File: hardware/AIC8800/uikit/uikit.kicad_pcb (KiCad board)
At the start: 2 copper layers, 50.8 x 69.2 mm, 48 parts, among them J1 Conn_01x20, J2 Conn_01x20, J3 Conn_01x10, J4 Conn_01x06, J5 USB_C_Receptacle_USB2.0, J6 Micro_SD_Card_Det, J7 PJ-393-USA, U1 AIC1000A, U2 CH340N, U3 NS8002

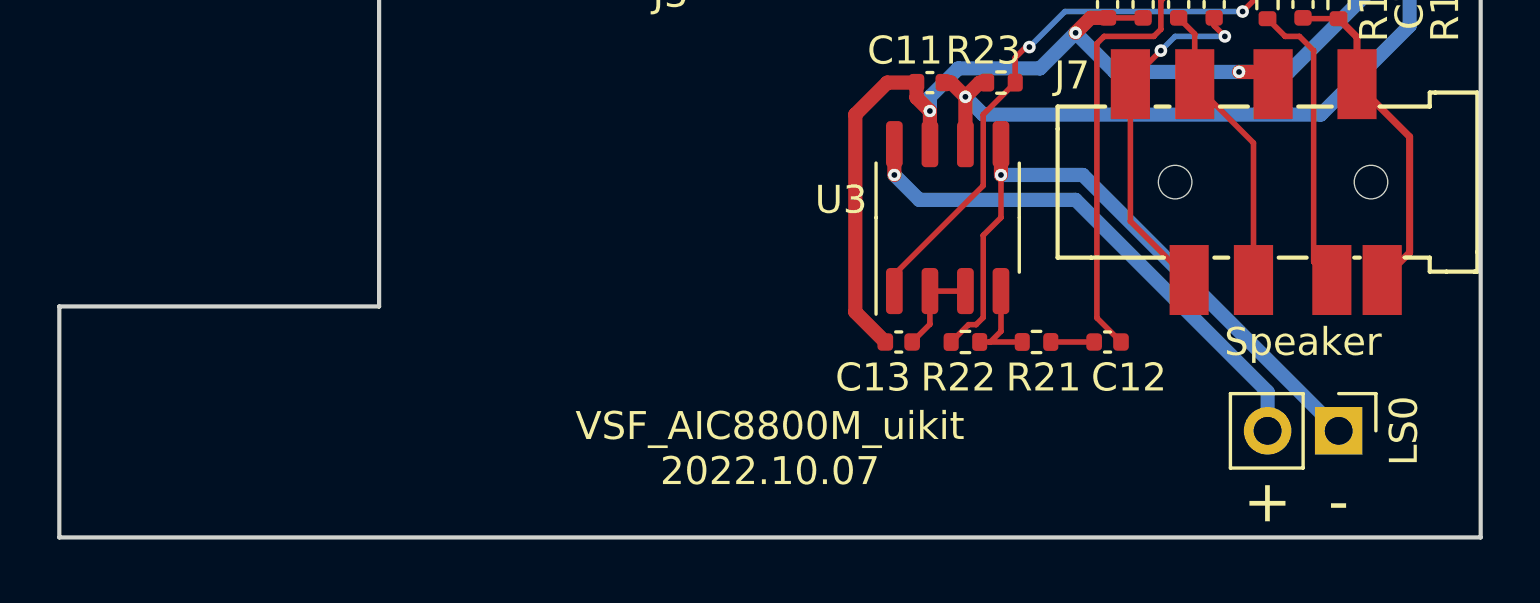
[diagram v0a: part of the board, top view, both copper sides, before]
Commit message: [hardware/aic8800/uikit] update microphone position
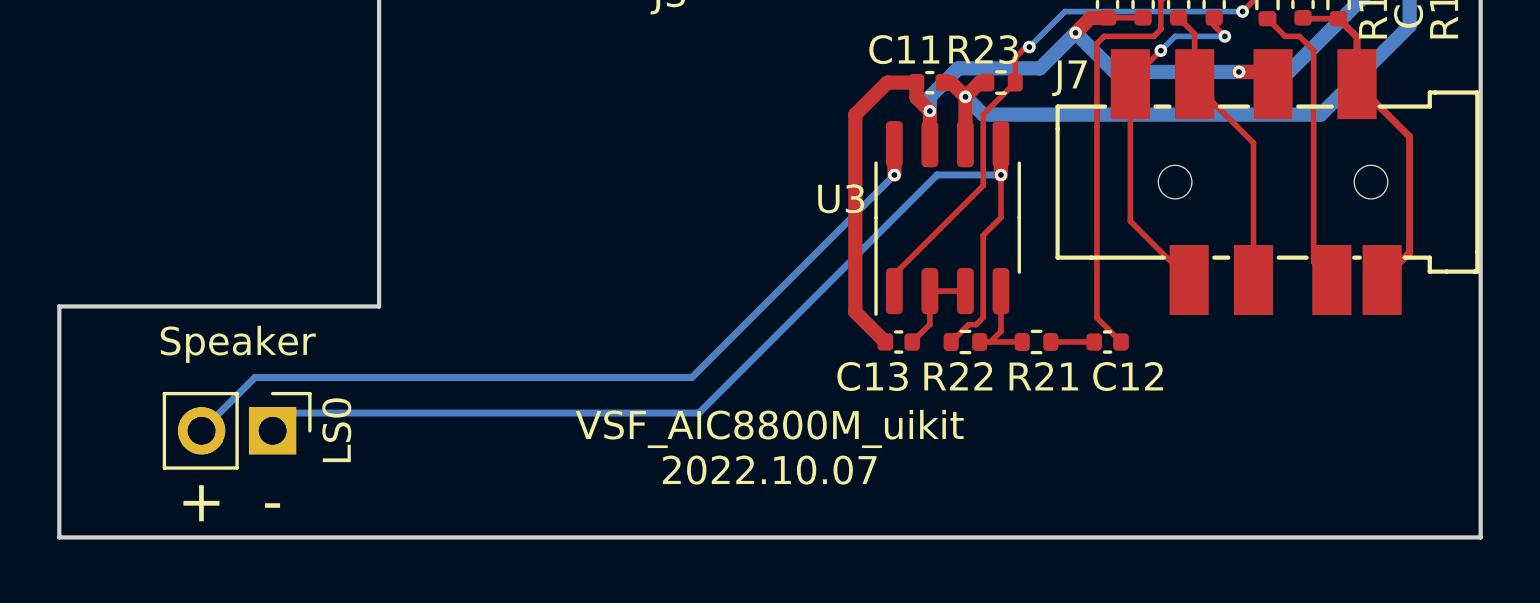
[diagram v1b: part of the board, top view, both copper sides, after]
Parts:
- moved LS0 38.1 mm to (210.8, 154.3)
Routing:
- net Net-(LS0-Pad1): track 23.8 -> 37.8 mm
- net Net-(LS0-Pad2): track 19.0 -> 29.6 mm
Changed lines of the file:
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@@
   )
   (footprint "Connector_PinHeader_2.54mm:PinHeader_1x02_P2.54mm_Vertical" (layer "F.Cu")
-    (at 248.925 154.305 -90)
+    (at 210.825 154.305 -90)
     (descr "Through hole straight pin header, 1x02, 2.54mm pitch, single row")
     (tags "Through hole pin header THT 1x02 2.54mm single row")
@@
   (gr_line (start 254 88.9) (end 254 119.888) (layer "Edge.Cuts") (width 0.15))
   (gr_line (start 203.2 132.08) (end 214.63 132.08) (layer "Edge.Cuts") (width 0.15))
-  (gr_text "+" (at 246.38 156.845) (layer "F.SilkS")
+  (gr_text "+" (at 208.28 156.845) (layer "F.SilkS")
     (effects (font (size 1.5 1.5) (thickness 0.3)))
   )
-  (gr_text "-" (at 248.92 156.845) (layer "F.SilkS")
+  (gr_text "-" (at 210.82 156.845) (layer "F.SilkS")
     (effects (font (size 1.5 1.5) (thickness 0.3)))
   )
-  (gr_text "Speaker" (at 247.65 151.13) (layer "F.SilkS")
+  (gr_text "Speaker" (at 209.55 151.13) (layer "F.SilkS")
     (effects (font (size 1 1) (thickness 0.15)))
   )
@@
   (segment (start 235.966 150.51) (end 235.695 150.51) (width 0.2) (layer "F.Cu") (net 73))
   (via (at 236.855 145.161) (size 0.45212) (drill 0.2032) (layers "F.Cu" "B.Cu") (net 73))
-  (segment (start 248.925 154.305) (end 239.781 145.161) (width 0.508) (layer "B.Cu") (net 73))
-  (segment (start 239.781 145.161) (end 236.855 145.161) (width 0.508) (layer "B.Cu") (net 73))
+  (segment (start 211.46 153.67) (end 226.06 153.67) (width 0.25) (layer "B.Cu") (net 73))
+  (segment (start 210.825 154.305) (end 211.46 153.67) (width 0.25) (layer "B.Cu") (net 73))
+  (segment (start 226.06 153.67) (end 234.569 145.161) (width 0.25) (layer "B.Cu") (net 73))
+  (segment (start 234.569 145.161) (end 236.855 145.161) (width 0.25) (layer "B.Cu") (net 73))
   (segment (start 233.045 144.06) (end 233.045 145.161) (width 0.508) (layer "F.Cu") (net 74))
   (via (at 233.045 145.161) (size 0.45212) (drill 0.2032) (layers "F.Cu" "B.Cu") (net 74))
-  (segment (start 233.934 146.05) (end 233.045 145.161) (width 0.508) (layer "B.Cu") (net 74))
-  (segment (start 239.522 146.05) (end 233.934 146.05) (width 0.508) (layer "B.Cu") (net 74))
-  (segment (start 246.385 154.305) (end 246.385 152.913) (width 0.508) (layer "B.Cu") (net 74))
-  (segment (start 246.385 152.913) (end 239.522 146.05) (width 0.508) (layer "B.Cu") (net 74))
+  (segment (start 210.19 152.4) (end 225.806 152.4) (width 0.25) (layer "B.Cu") (net 74))
+  (segment (start 208.285 154.305) (end 210.19 152.4) (width 0.25) (layer "B.Cu") (net 74))
+  (segment (start 225.806 152.4) (end 233.045 145.161) (width 0.25) (layer "B.Cu") (net 74))
   (segment (start 236.474 151.13) (end 236.095 151.13) (width 0.2) (layer "F.Cu") (net 75))
   (segment (start 237.615 151.13) (end 236.474 151.13) (width 0.2) (layer "F.Cu") (net 75))

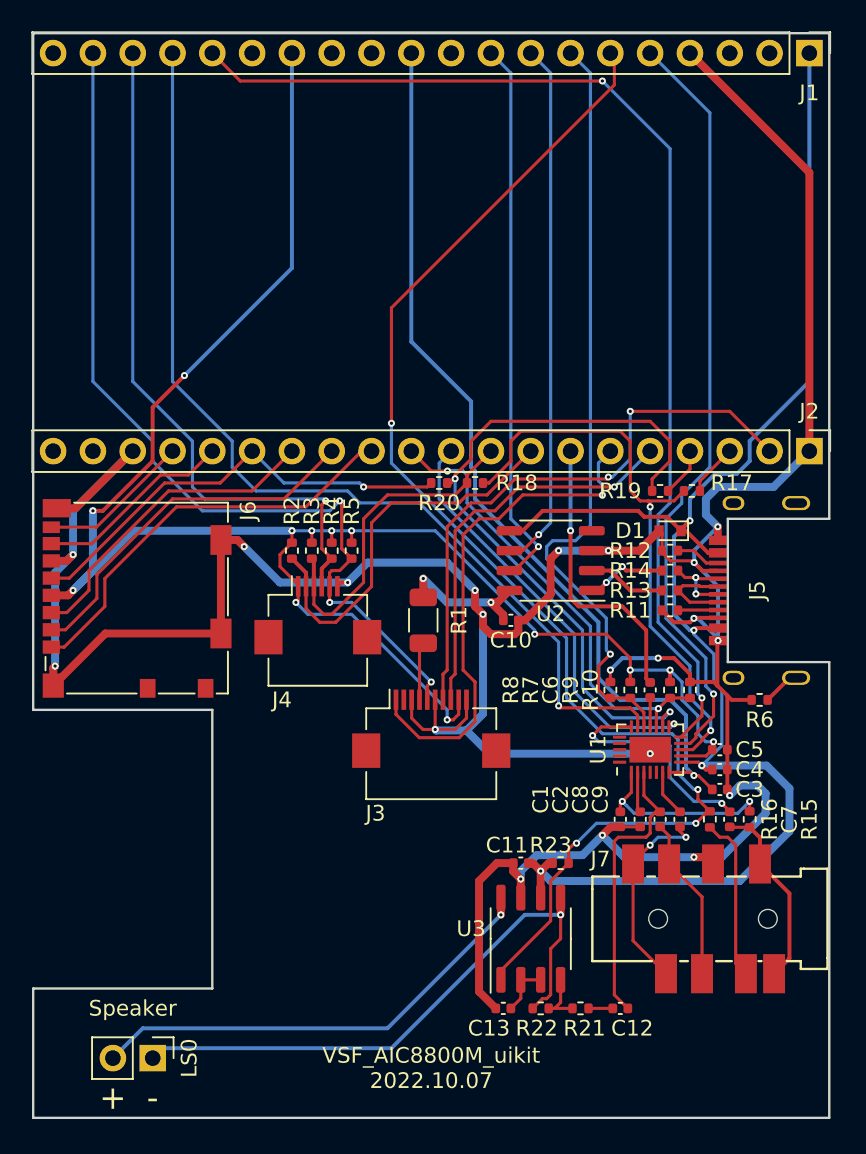
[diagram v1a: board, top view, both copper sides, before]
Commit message: [hardware/aic8800m_uikit] add bootloader button
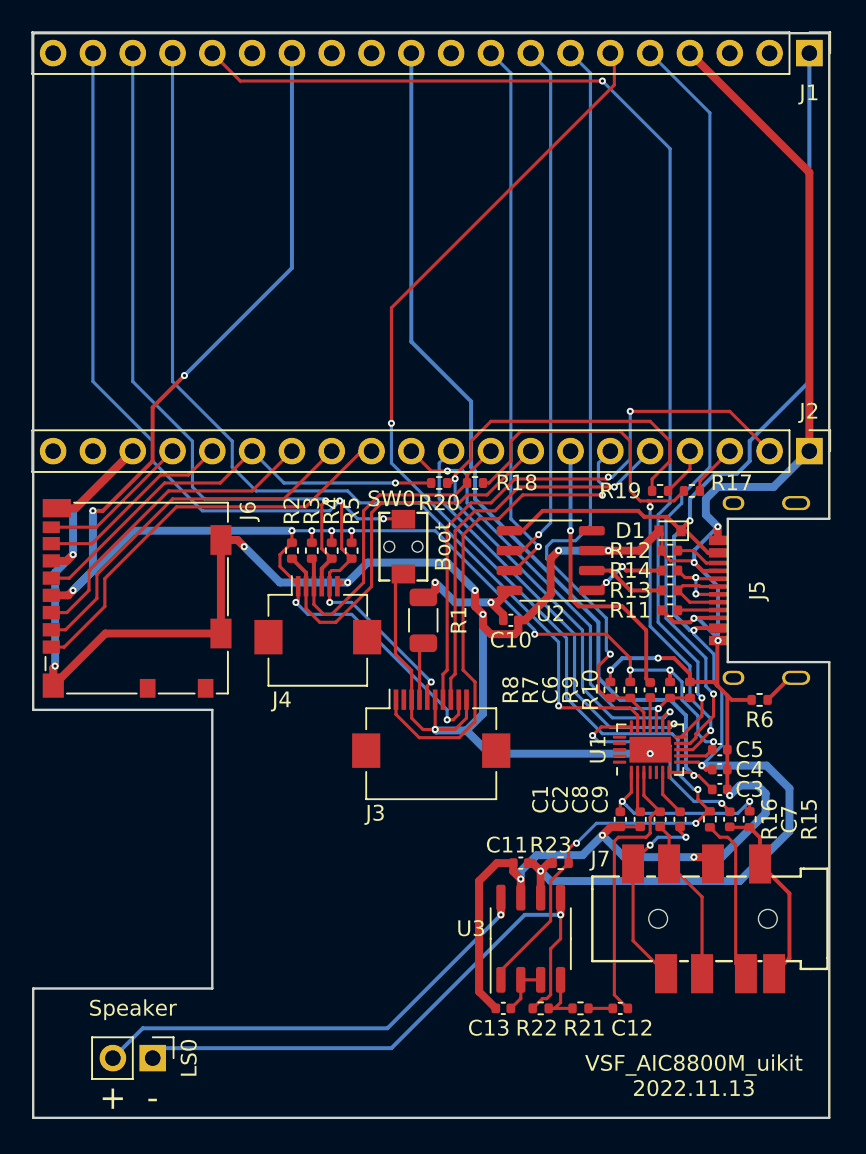
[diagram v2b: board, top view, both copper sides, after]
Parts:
- added SW0: SW_Push, VSF:Key_2Pin_2.9X4.3, F.Cu at (226.8, 121.7)
- C11, C13: value 0.1uF -> 1.0uF
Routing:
- net GND: track 233.6 -> 242.3 mm
- net /B7: track 58.6 -> 63.2 mm, vias 3 -> 4
- net /USB_3V: track 9.12 -> 8.51 mm
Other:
- board text added: "Boot"
- board text added: "VSF_AIC8800M_uikit 2022.11.13"
- board text removed: "VSF_AIC8800M_uikit 2022.10.07"

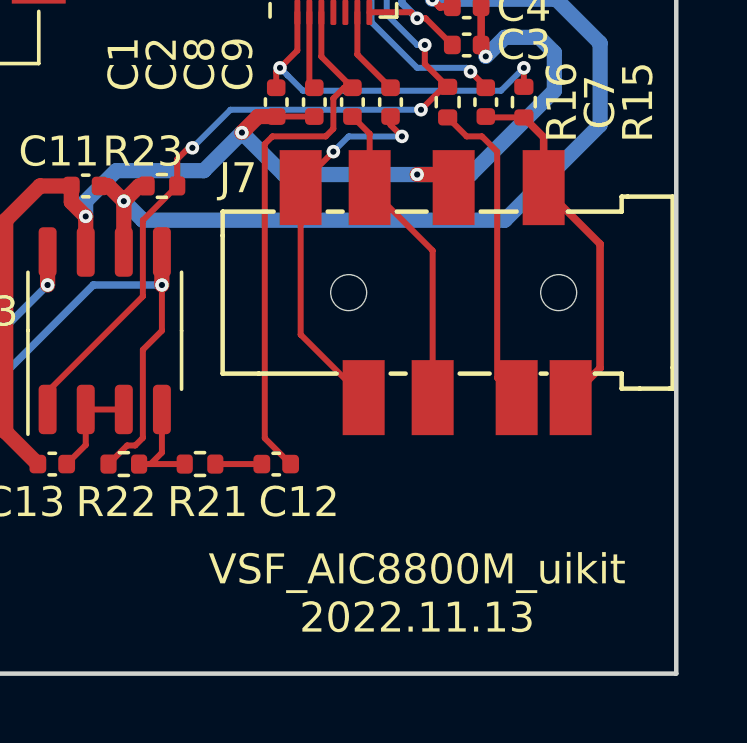
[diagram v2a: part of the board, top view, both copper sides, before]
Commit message: [hardware/aic8800m/uikit] add GND pin
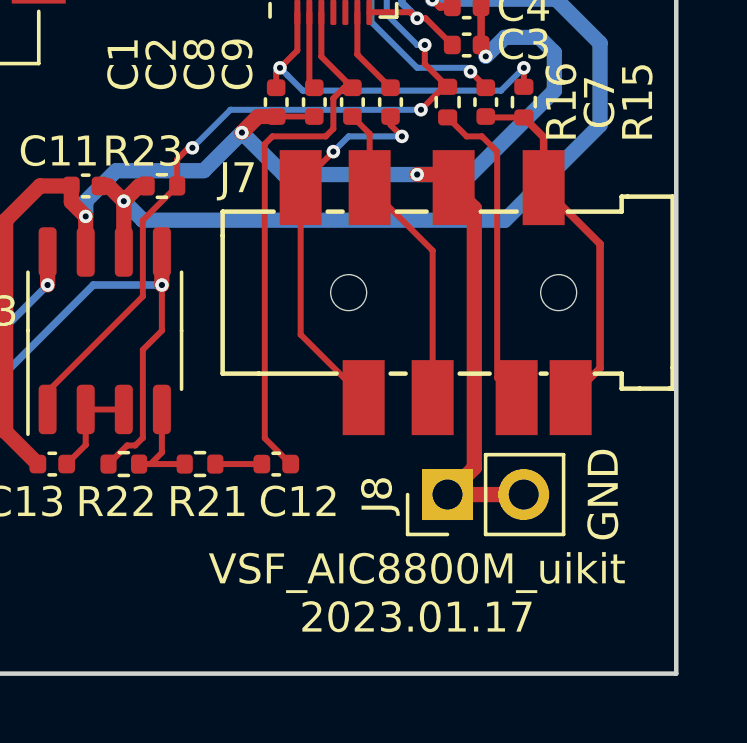
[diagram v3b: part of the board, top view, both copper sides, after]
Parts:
- added J8: Conn_01x02, Connector_PinHeader_2.54mm:PinHeader_1x02_P2.54mm_Vertical, F.Cu at (246.4, 152.1)
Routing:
- net GND: track 242.3 -> 255.7 mm
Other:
- board text added: "GND"
- board text added: "VSF_AIC8800M_uikit 2023.01.17"
- board text removed: "VSF_AIC8800M_uikit 2022.11.13"
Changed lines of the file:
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@@
+    )
+  )
+  (footprint "Connector_PinHeader_2.54mm:PinHeader_1x02_P2.54mm_Vertical" (layer "F.Cu")
+    (at 246.375 152.146 90)
+    (descr "Through hole straight pin header, 1x02, 2.54mm pitch, single row")
+    (tags "Through hole pin header THT 1x02 2.54mm single row")
+    (property "Sheetfile" "uikit.kicad_sch")
+    (property "Sheetname" "")
+    (attr through_hole)
+    (fp_text reference "J8" (at 0 -2.33 90) (layer "F.SilkS")
+      (effects (font (size 1 1) (thickness 0.15)))
+    )
+    (fp_text value "Conn_01x02" (at 0 4.87 90) (layer "F.Fab") hide
+      (effects (font (size 1 1) (thickness 0.15)))
+    )
+    (fp_text user "${REFERENCE}" (at 0 1.27) (layer "F.Fab")
+      (effects (font (size 1 1) (thickness 0.15)))
+    )
+    (fp_line (start -1.33 3.87) (end 1.33 3.87) (layer "F.SilkS") (width 0.12))
+    (fp_line (start 1.33 1.27) (end 1.33 3.87) (layer "F.SilkS") (width 0.12))
+    (fp_line (start -1.33 1.27) (end -1.33 3.87) (layer "F.SilkS") (width 0.12))
+    (fp_line (start -1.33 -1.33) (end 0 -1.33) (layer "F.SilkS") (width 0.12))
+    (fp_line (start -1.33 1.27) (end 1.33 1.27) (layer "F.SilkS") (width 0.12))
+    (fp_line (start -1.33 0) (end -1.33 -1.33) (layer "F.SilkS") (width 0.12))
+    (fp_line (start -1.8 -1.8) (end -1.8 4.35) (layer "F.CrtYd") (width 0.05))
+    (fp_line (start 1.8 4.35) (end 1.8 -1.8) (layer "F.CrtYd") (width 0.05))
+    (fp_line (start -1.8 4.35) (end 1.8 4.35) (layer "F.CrtYd") (width 0.05))
+    (fp_line (start 1.8 -1.8) (end -1.8 -1.8) (layer "F.CrtYd") (width 0.05))
+    (fp_line (start 1.27 -1.27) (end 1.27 3.81) (layer "F.Fab") (width 0.1))
+    (fp_line (start -1.27 -0.635) (end -0.635 -1.27) (layer "F.Fab") (width 0.1))
+    (fp_line (start -0.635 -1.27) (end 1.27 -1.27) (layer "F.Fab") (width 0.1))
+    (fp_line (start -1.27 3.81) (end -1.27 -0.635) (layer "F.Fab") (width 0.1))
+    (fp_line (start 1.27 3.81) (end -1.27 3.81) (layer "F.Fab") (width 0.1))
+    (pad "1" thru_hole rect (at 0 0 90) (size 1.7 1.7) (drill 1) (layers *.Cu *.Mask)
+      (net 1 "GND") (pinfunction "Pin_1") (pintype "passive"))
+    (pad "2" thru_hole oval (at 0 2.54 90) (size 1.7 1.7) (drill 1) (layers *.Cu *.Mask)
+      (net 1 "GND") (pinfunction "Pin_2") (pintype "passive"))
+    (model "${KICAD6_3DMODEL_DIR}/Connector_PinHeader_2.54mm.3dshapes/PinHeader_1x02_P2.54mm_Vertical.wrl"
+      (offset (xyz 0 0 0))
+      (scale (xyz 1 1 1))
+      (rotate (xyz 0 0 0))
     )
   )
@@
     (effects (font (size 1.5 1.5) (thickness 0.3)))
   )
+  (gr_text "GND" (at 251.587 152.146 90) (layer "F.SilkS")
+    (effects (font (size 1 1) (thickness 0.15)))
+  )
   (gr_text "-" (at 210.82 156.845) (layer "F.SilkS")
     (effects (font (size 1.5 1.5) (thickness 0.3)))
@@
     (effects (font (size 1 1) (thickness 0.15)))
   )
-  (gr_text "VSF_AIC8800M_uikit\n2022.11.13" (at 245.364 155.448) (layer "F.SilkS")
+  (gr_text "VSF_AIC8800M_uikit\n2023.01.17" (at 245.364 155.448) (layer "F.SilkS")
     (effects (font (size 1 1) (thickness 0.15)))
   )
@@
   (segment (start 249.045 131.445) (end 247.777 131.445) (width 0.25) (layer "F.Cu") (net 1))
   (segment (start 246.888 120.396) (end 246.888 121.2469) (width 0.508) (layer "F.Cu") (net 1))
+  (segment (start 248.915 152.146) (end 246.375 152.146) (width 0.508) (layer "F.Cu") (net 1))
   (segment (start 227.35 131.43) (end 227.35 129.56) (width 0.2) (layer "F.Cu") (net 1))
   (segment (start 245.364 141.478) (end 246.143 141.478) (width 0.508) (layer "F.Cu") (net 1))
@@
   (segment (start 242.57 134.62) (end 242.57 134.874) (width 0.2) (layer "F.Cu") (net 1))
   (segment (start 243.33 121.92) (end 243.33 122.045) (width 0.2) (layer "F.Cu") (net 1))
+  (segment (start 247.269 142.604) (end 247.269 151.252) (width 0.508) (layer "F.Cu") (net 1))
   (segment (start 247.495 137.16) (end 247.495 135.89) (width 0.254) (layer "F.Cu") (net 1))
+  (segment (start 246.58 141.915) (end 247.269 142.604) (width 0.508) (layer "F.Cu") (net 1))
   (segment (start 233.934 127.254) (end 232.41 127.254) (width 0.508) (layer "F.Cu") (net 1))
+  (segment (start 247.269 151.252) (end 246.375 152.146) (width 0.508) (layer "F.Cu") (net 1))
   (segment (start 245.11 130.3) (end 245.11 129.794) (width 0.254) (layer "F.Cu") (net 1))
   (segment (start 207.804 127.208) (end 204.479 130.533) (width 0.508) (layer "F.Cu") (net 1))
